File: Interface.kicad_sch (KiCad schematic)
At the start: 1 part, among them U3 USB3300-EZK-TR

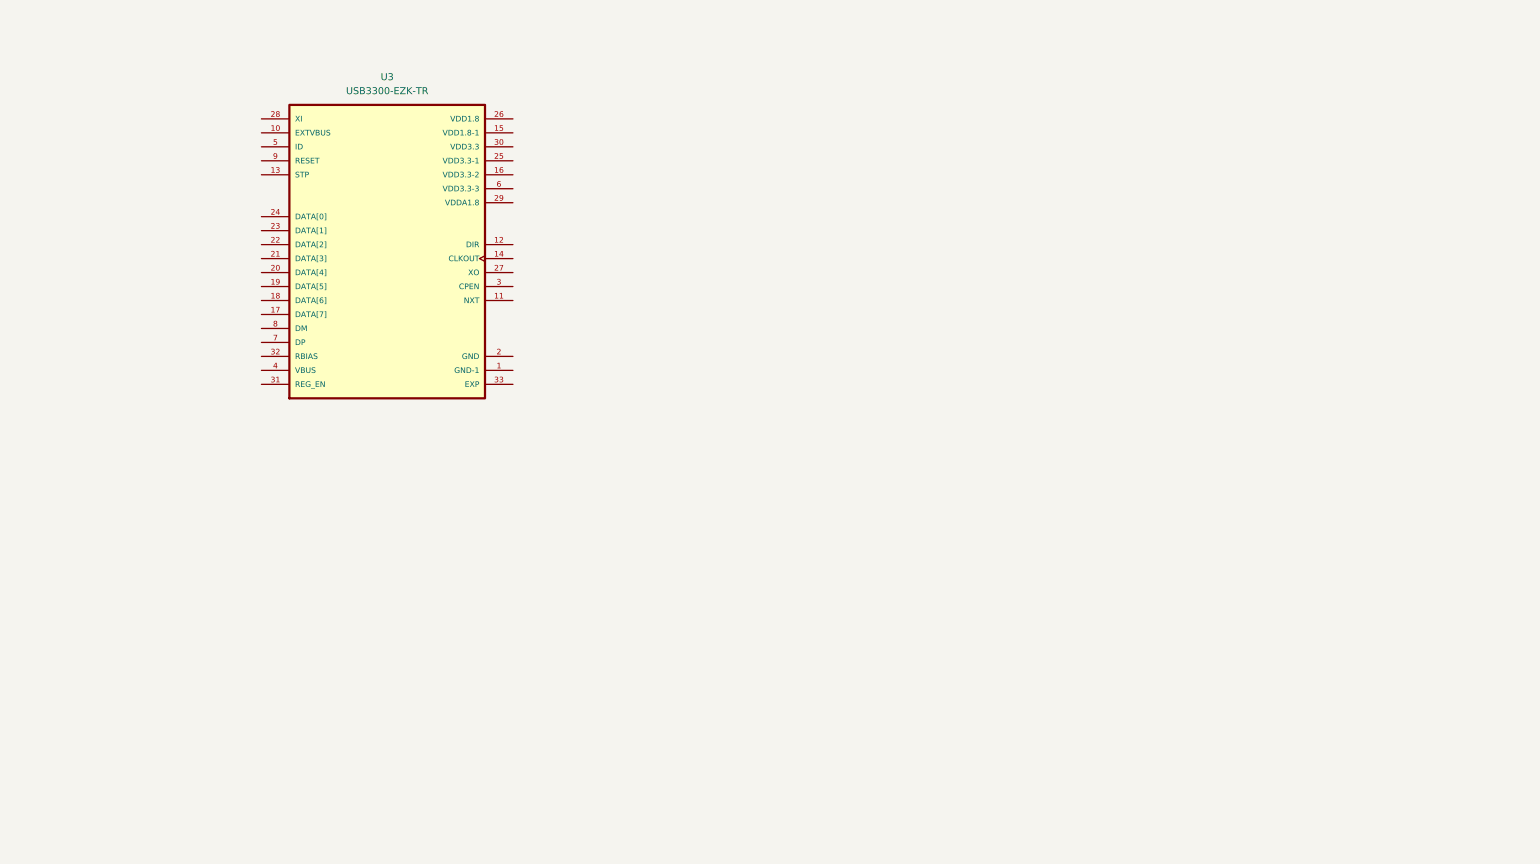
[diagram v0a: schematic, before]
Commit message: added USB (needs revision), fixed medium voltage rail
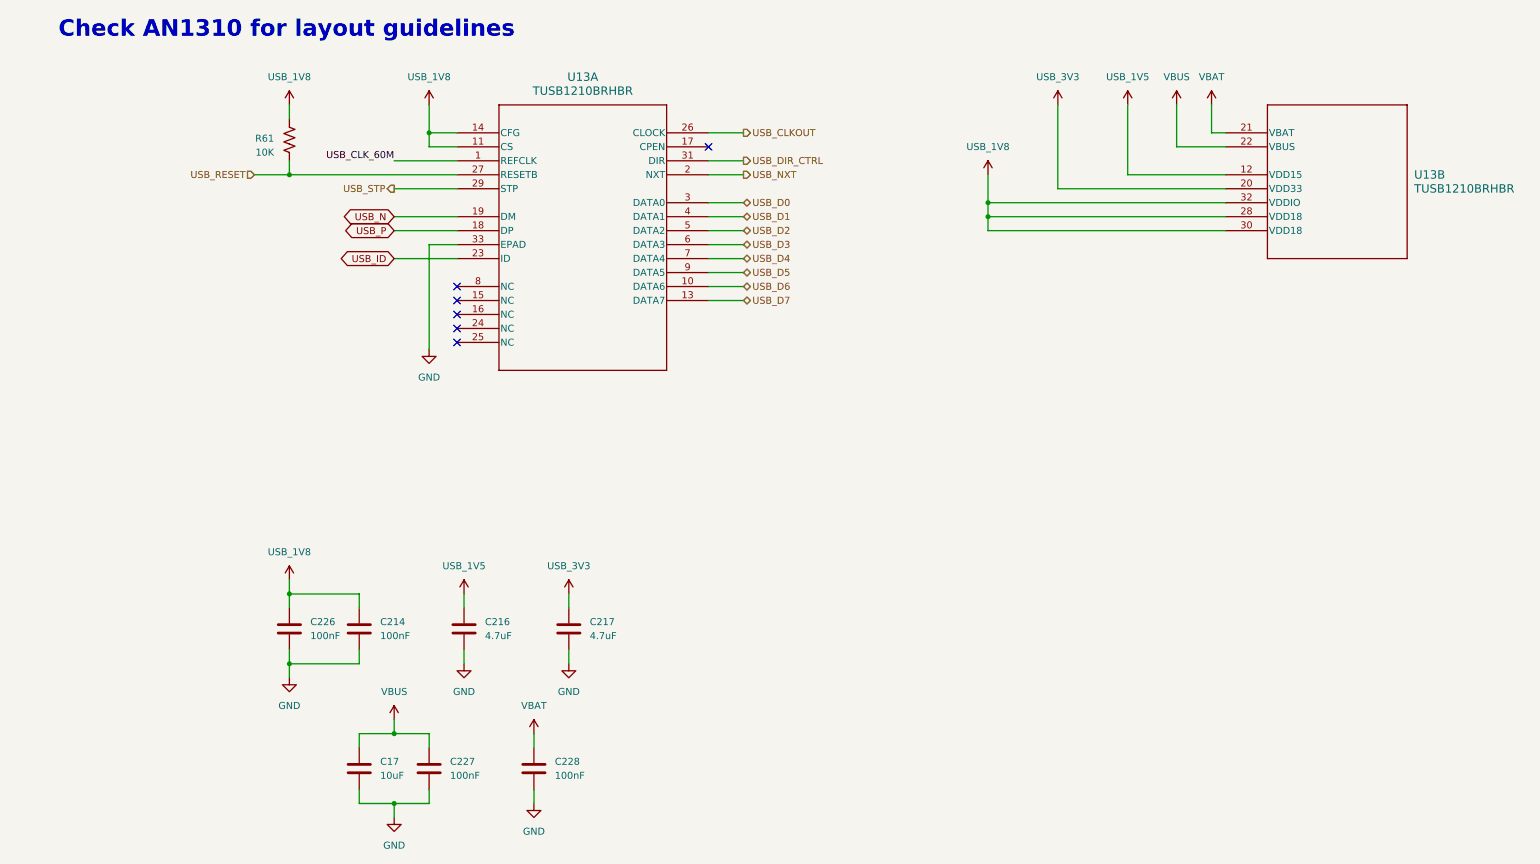
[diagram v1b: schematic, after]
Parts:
- removed U3: USB3300-EZK-TR, USB3300-EZK-TR:QFN50P500X500X100-33N, symbol USB3300-EZK-TR:USB3300-EZK-TR
- added C17: 10uF, symbol Device:C
- added C214, C226, C227, C228: 100nF, symbol Device:C
- added C216, C217: 4.7uF, symbol Device:C
- added R61: 10K, symbol Device:R_US
- added U13: TUSB1210BRHBR, RHB32_3P45X3P45, symbol TUSB1210BRHBR:TUSB1210BRHBR
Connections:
- new net GND: C17.2, C214.1, C216.1, C217.1, C226.1, C227.1, C228.1, U13.33 (EPAD)
- new net USB_1V5: C216.2, U13.12 (VDD15)
- new net USB_1V8: C214.2, C226.2, R61.1, U13.11 (CS), U13.14 (CFG), U13.28 (VDD18), U13.30 (VDD18), U13.32 (VDDIO)
- new net USB_3V3: C217.2, U13.20 (VDD33)
- new net USB_CLKOUT: U13.26 (CLOCK)
- new net USB_CLK_60M: U13.1 (REFCLK)
- new net USB_D0: U13.3 (DATA0)
- new net USB_D1: U13.4 (DATA1)
- new net USB_D2: U13.5 (DATA2)
- new net USB_D3: U13.6 (DATA3)
- new net USB_D4: U13.7 (DATA4)
- new net USB_D5: U13.9 (DATA5)
- new net USB_D6: U13.10 (DATA6)
- new net USB_D7: U13.13 (DATA7)
- new net USB_DIR_CTRL: U13.31 (DIR)
- new net USB_ID: U13.23 (ID)
- new net USB_N: U13.19 (DM)
- new net USB_NXT: U13.2 (NXT)
- new net USB_P: U13.18 (DP)
- new net USB_RESET: R61.2, U13.27 (RESETB)
- new net USB_STP: U13.29 (STP)
- new net VBAT: C228.2, U13.21 (VBAT)
- new net VBUS: C17.1, C227.2, U13.22 (VBUS)
- no-connect marks 0 -> 6
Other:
- note added: "Check AN1310 for layout guidelines"

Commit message: almost finished, phew! just dd +/- 5v rails, connect the SDIO & power enable pins and figure out the rest of the clocking chain
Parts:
- added C164, C166, C183: 100nF, symbol Device:C
- added C165: 1uF, symbol Device:C
- added FB9: BLM15AG601SN1D, symbol Device:FerriteBead
- added J3: 47352-1001, 47352-1001:MOLEX_47352-1001, symbol 47352-1001:47352-1001
- added R65: 100K, symbol Device:R_US
- added U10: USBLC6-2SC6, Package_TO_SOT_SMD:SOT-23-6, symbol Power_Protection:USBLC6-2SC6
- added U24: NVT4858HKZ, NVT4858_NXP, symbol NVT4858HKZ:NVT4858HKZ
- added Y2: TG-5006CG-12H_26.0000M3, TG5006CG12H260000M3, symbol TG-5006CG-12H_26_0000M3:TG-5006CG-12H_26.0000M3
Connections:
- net USB_CLK_60M is gone; now on net GND: U13.1 (REFCLK)
- net VBAT is gone; now on net USB_3V3: C228.2, U13.21 (VBAT)
- net GND: now also C164.2, C165.2, C166.2, C183.2, J3.6 (VSS), J3.S1 (SHIELD), J3.S2 (SHIELD__1), J3.S3 (SHIELD__2), J3.S4 (SHIELD__3), U10.2 (GND), U24.7 (GND), Y2.2 (GND)
- net USB_1V8: now also FB9.1, R65.1, U24.14 (VCCB)
- net USB_N: now also U10.1 (I/O1); no longer U13.19 (DM)
- net USB_P: now also U10.3 (I/O2); no longer U13.18 (DP)
- net VBUS: now also U10.5 (VBUS)
- net USB_CLKOUT renamed USB_26MHZ
- net USB_26MHZ: now also Y2.3 (OUT)
- new net SD_3V3: C164.1, C165.1, C166.1, J3.4 (VDD), U24.15 (VCCA)
- new net SD_CLK: U24.8 (CLKB)
- new net SD_CLK_PRE: J3.5 (CLK), U24.5 (CLKA)
- new net SD_CMD: U24.13 (CMDB)
- new net SD_CMD_PRE: J3.3 (CMD), U24.16 (CMDA)
- new net SD_DAT0: U24.10 (DAT0B)
- new net SD_DAT0_PRE: J3.7 (DATA0), U24.3 (DAT0A)
- new net SD_DAT1: U24.9 (DAT1B)
- new net SD_DAT1_PRE: J3.8 (DATA1), U24.4 (DAT1A)
- new net SD_DAT2: U24.12 (DAT2B)
- new net SD_DAT2_PRE: J3.1 (DATA2), U24.1 (DAT2A)
- new net SD_DAT3: U24.11 (DAT3B)
- new net SD_DAT3_PRE: J3.2 (CD/DATA3), U24.2 (DAT3A)
- new net SD_DETECT: J3.SW, R65.2
- new net USB_OSC_1V8: C183.1, FB9.2, Y2.4 (VCC)
- new net USB_PRE_N: U10.6 (I/O1), U13.19 (DM)
- new net USB_PRE_P: U10.4 (I/O2), U13.18 (DP)
- no-connect marks 6 -> 8
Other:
- note added: "3V3 & 1V5 are the outputs of internal LDOs"
- moved on the sheet: C17, C214, C216, C217, C226, C227, C228

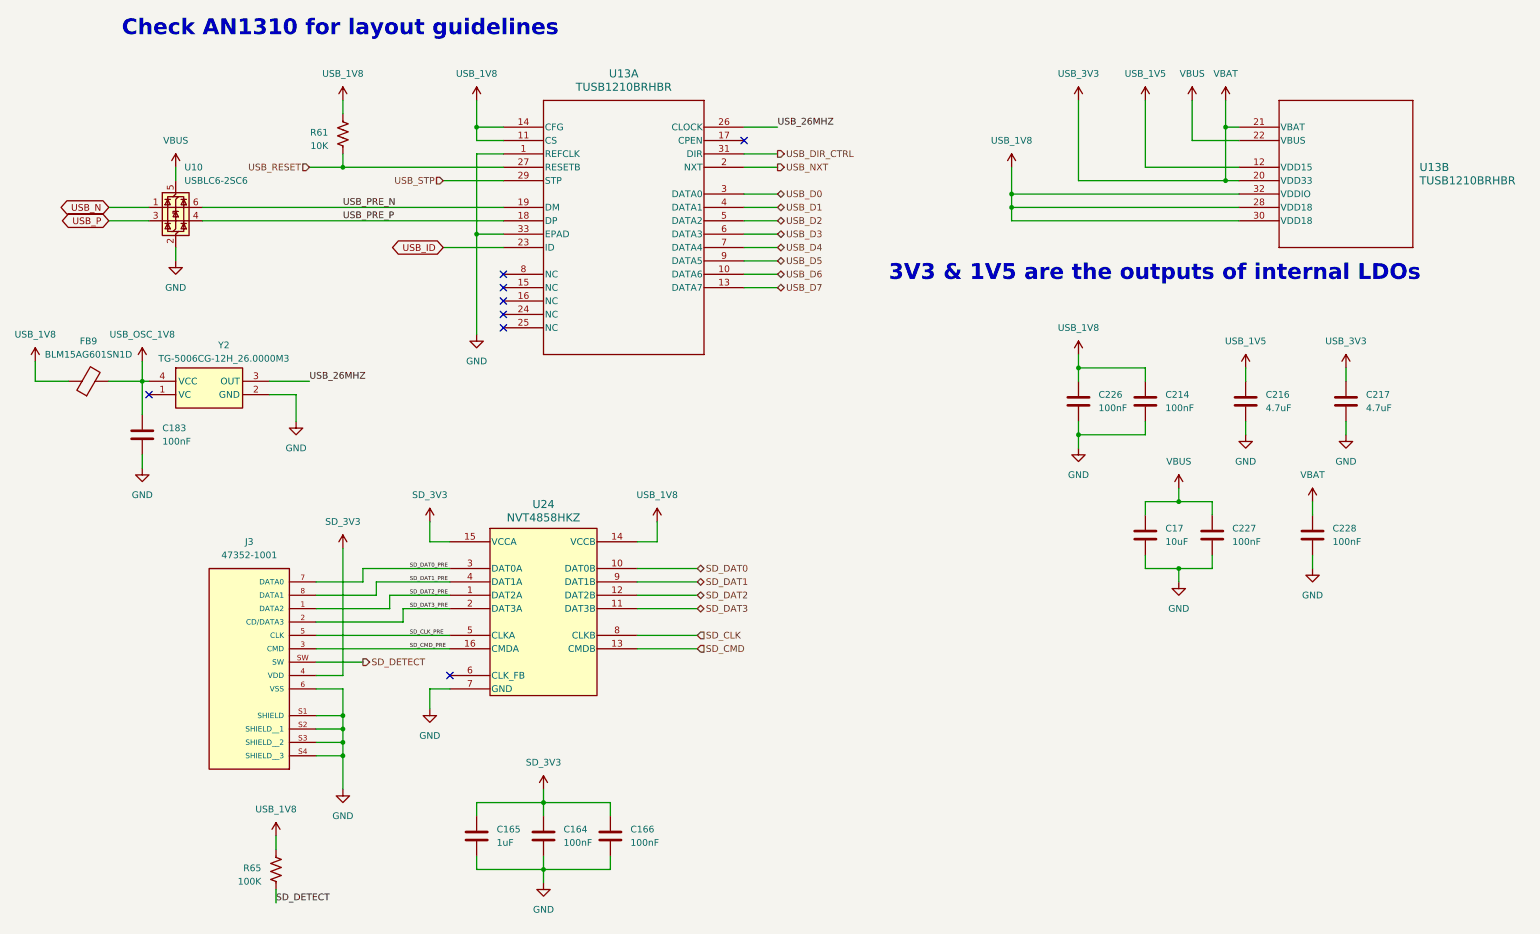
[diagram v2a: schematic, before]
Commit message: HDMI was requested so add it and give the signal chain a final revision
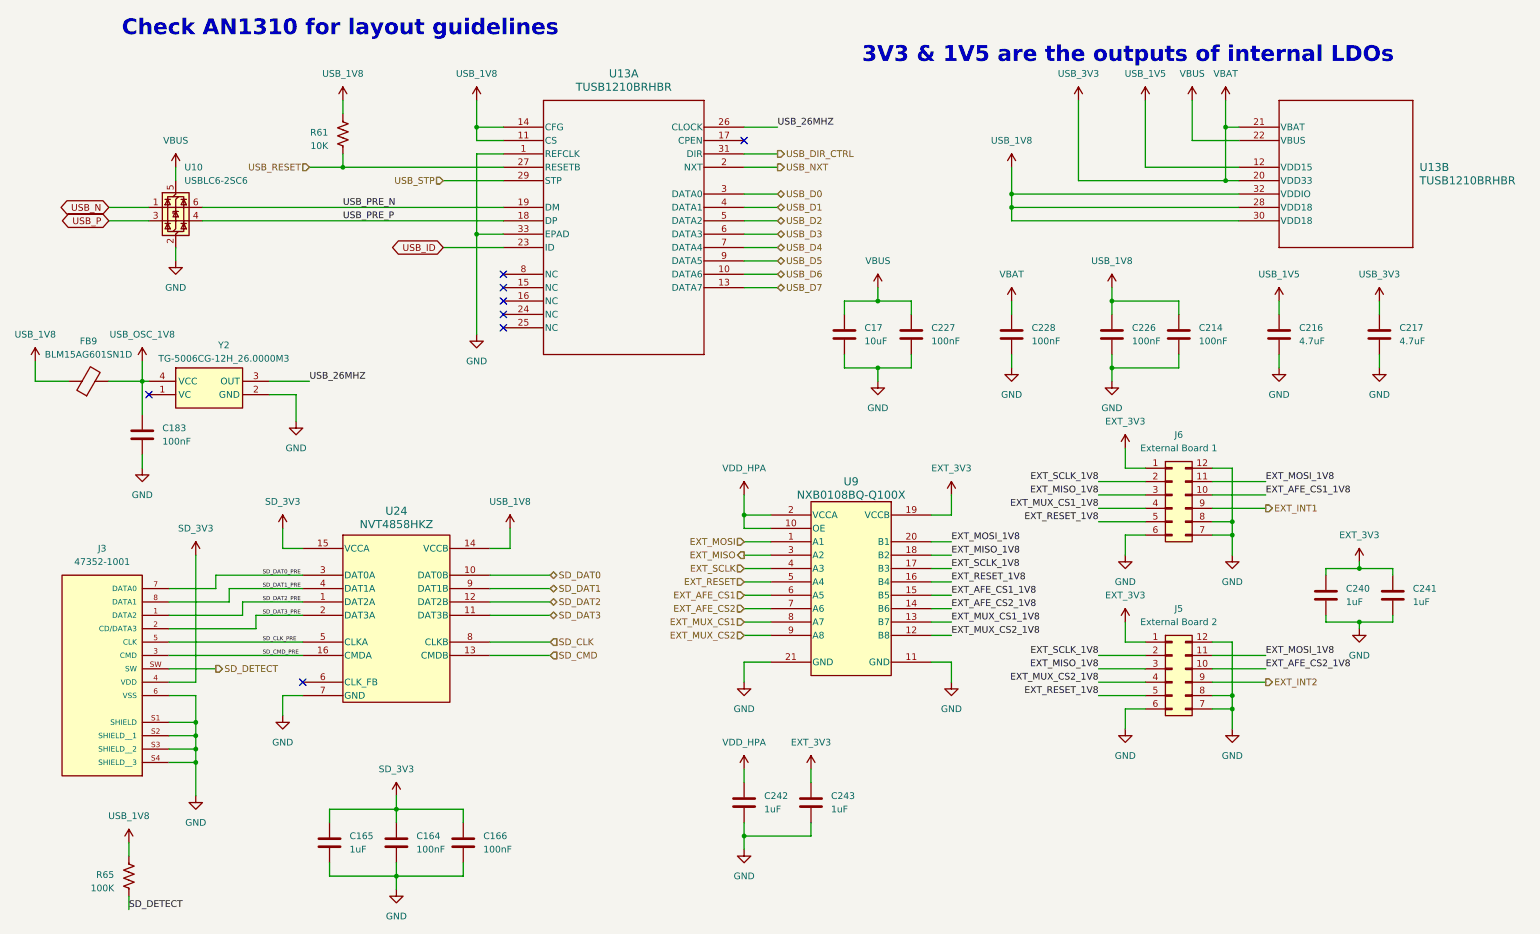
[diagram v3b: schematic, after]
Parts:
- added C240, C241, C242, C243: 1uF, symbol Device:C
- added J5: External Board 2, symbol Connector_Generic:Conn_02x06_Counter_Clockwise
- added J6: External Board 1, symbol Connector_Generic:Conn_02x06_Counter_Clockwise
- added U9: NXB0108BQ-Q100X, DHVQFN20_SOT764-1_NEX, symbol NXB0108BQ-Q100X:NXB0108BQ-Q100X
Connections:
- net GND: now also C240.2, C241.2, C242.2, C243.2, J5.12 (Pin_12), J5.6 (Pin_6), J5.7 (Pin_7), J5.8 (Pin_8), J6.12 (Pin_12), J6.6 (Pin_6), J6.7 (Pin_7), J6.8 (Pin_8), U9.11 (GND), U9.21 (GND)
- new net EXT_3V3: C240.1, C241.1, C243.1, J5.1 (Pin_1), J6.1 (Pin_1), U9.19 (VCCB)
- new net EXT_AFE_CS1: U9.6 (A5)
- new net EXT_AFE_CS1_1V8: J6.10 (Pin_10), U9.15 (B5)
- new net EXT_AFE_CS2: U9.7 (A6)
- new net EXT_AFE_CS2_1V8: J5.10 (Pin_10), U9.14 (B6)
- new net EXT_INT1: J6.9 (Pin_9)
- new net EXT_INT2: J5.9 (Pin_9)
- new net EXT_MISO: U9.3 (A2)
- new net EXT_MISO_1V8: J5.3 (Pin_3), J6.3 (Pin_3), U9.18 (B2)
- new net EXT_MOSI: U9.1 (A1)
- new net EXT_MOSI_1V8: J5.11 (Pin_11), J6.11 (Pin_11), U9.20 (B1)
- new net EXT_MUX_CS1: U9.8 (A7)
- new net EXT_MUX_CS1_1V8: J6.4 (Pin_4), U9.13 (B7)
- new net EXT_MUX_CS2: U9.9 (A8)
- new net EXT_MUX_CS2_1V8: J5.4 (Pin_4), U9.12 (B8)
- new net EXT_RESET: U9.5 (A4)
- new net EXT_RESET_1V8: J5.5 (Pin_5), J6.5 (Pin_5), U9.16 (B4)
- new net EXT_SCLK: U9.4 (A3)
- new net EXT_SCLK_1V8: J5.2 (Pin_2), J6.2 (Pin_2), U9.17 (B3)
- new net VDD_HPA: C242.1, U9.10 (OE), U9.2 (VCCA)
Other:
- moved on the sheet: C164, C165, C166, C17, C214, C216, C217, C226, C227, C228, J3, R65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

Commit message: ALL IS DONE EXCEPT HDMI PLEASE HELP
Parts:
- removed C17: 10uF, symbol Device:C
- removed C183: 100nF, symbol Device:C
- removed FB9: BLM15AG601SN1D, symbol Device:FerriteBead
- removed Y2: TG-5006CG-12H_26.0000M3, TG5006CG12H260000M3, symbol TG-5006CG-12H_26_0000M3:TG-5006CG-12H_26.0000M3
- added C246, C247, C248, C249, C250, C251, C252, C253, C254, C255, C256, C257, C258, C259, C260, C261: 100nF, symbol Device:C
- added C47: 47uF, symbol Device:C
- added CR1: DT1240A-08LP3810-7, U-DFN3810-9_TYPE_B_DIO, symbol DT1240A-08LP3810-7:DT1240A-08LP3810-7
- added J4: 2086581001, 2086581001:MOLEX_2086581001, symbol 2086581001:2086581001
- added J7: TYPE-C-31-M-12, TYPE-C-31-M-12:HRO_TYPE-C-31-M-12, symbol TYPE-C-31-M-12:TYPE-C-31-M-12
- added JP16: HPD_INV_PUP, U-DFN3810-9_TYPE_B_DIO, symbol Jumper:SolderJumper_2_Open
- added R106, R107, R67, R68, R85, R86, R87, R88: 10K, symbol Device:R_US
- added R109: 50R, symbol Device:R_US
- added R110, R111: 5.1K, symbol Device:R_US
- added R17: 4.02K, symbol Device:R_US
- added R69, R70, R83, R84: 3.3k, symbol Device:R_US
- added U18: SN75DP139RSBR, RSB40_3P15X3P15, symbol SN75DP139RSBR:SN75DP139RSBR
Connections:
- net GND: now also C246.2, C247.2, C248.2, C249.2, C250.2, C251.2, C252.2, C253.2, C47.2, CR1.3 (GND), J7.A1_B12 (GND), J7.B1_A12 (GND), J7.S1 (SHIELD), J7.S2 (SHIELD), J7.S3 (SHIELD), J7.S4 (SHIELD), R106.2, R110.2, R111.2, R17.2, R68.2, R86.2, R88.2, U18.41 (EPAD)
- net SD_3V3: now also U24.14 (VCCB); no longer U24.15 (VCCA)
- net SD_CLK: now also U24.5 (CLKA); no longer U24.8 (CLKB)
- net SD_CLK_PRE: now also U24.8 (CLKB); no longer U24.5 (CLKA)
- net SD_CMD: now also U24.16 (CMDA); no longer U24.13 (CMDB)
- net SD_CMD_PRE: now also U24.13 (CMDB); no longer U24.16 (CMDA)
- net SD_DAT0: now also U24.3 (DAT0A); no longer U24.10 (DAT0B)
- net SD_DAT0_PRE: now also U24.10 (DAT0B); no longer U24.3 (DAT0A)
- net SD_DAT1: now also U24.4 (DAT1A); no longer U24.9 (DAT1B)
- net SD_DAT1_PRE: now also U24.9 (DAT1B); no longer U24.4 (DAT1A)
- net SD_DAT2: now also U24.1 (DAT2A); no longer U24.12 (DAT2B)
- net SD_DAT2_PRE: now also U24.12 (DAT2B); no longer U24.1 (DAT2A)
- net SD_DAT3: now also U24.2 (DAT3A); no longer U24.11 (DAT3B)
- net SD_DAT3_PRE: now also U24.11 (DAT3B); no longer U24.2 (DAT3A)
- net USB_1V8: now also U24.15 (VCCA); no longer U24.14 (VCCB)
- net USB_26MHZ: now also R109.1; no longer U13.26 (CLOCK)
- net USB_N: now also J7.A7 (DN1), J7.B7 (DN2)
- net USB_P: now also J7.A6 (DP1), J7.B6 (DP2)
- net VBUS: now also C47.1, J7.A4_B9 (VBUS), J7.B4_A9 (VBUS)
- new net: U18.11 (NC), U18.20 (NC), U18.40 (NC)
- new net DP0_N: C255.1
- new net DP0_P: C254.1
- new net DP0_PRE_N: C255.2, U18.1 (IN_D1-)
- new net DP0_PRE_P: C254.2, U18.2 (IN_D1+)
- new net DP1_N: C257.1
- new net DP1_P: C256.1
- new net DP1_PRE_N: C257.2, U18.4 (IN_D2-)
- new net DP1_PRE_P: C256.2, U18.5 (IN_D2+)
- new net DP2_N: C259.1
- new net DP2_P: C258.1
- new net DP2_PRE_N: C259.2, U18.6 (IN_D3-)
- new net DP2_PRE_P: C258.2, U18.7 (IN_D3+)
- new net DP3_N: C261.1
- new net DP3_P: C260.1
- new net DP3_PRE_N: C261.2, U18.9 (IN_D4-)
- new net DP3_PRE_P: C260.2, U18.10 (IN_D4+)
- new net HDMI_3V3: C246.1, C247.1, C248.1, C249.1, C250.1, C251.1, C252.1, C253.1, JP16.1 (A), R107.1, R67.1, R69.1, R70.1, R85.1, R87.1, U18.12 (VCC), U18.19 (VCCC), U18.23 (VCC), U18.28 (VCC), U18.3 (VCC), U18.32 (VCC), U18.37 (VCC), U18.8 (VCC)
- new net HDMI_5V: R83.1, R84.1
- new net HDMI_D0_N: CR1.6 (LINE-7), U18.30 (OUT_D1-)
- new net HDMI_D0_P: CR1.5 (LINE-8), U18.29 (OUT_D1+)
- new net HDMI_D1_N: CR1.7 (LINE-5), U18.27 (OUT_D2-)
- new net HDMI_D1_P: CR1.4 (LINE-6), U18.26 (OUT_D2+)
- new net HDMI_D2_N: CR1.2 (LINE-3), U18.25 (OUT_D3-)
- new net HDMI_D2_P: CR1.8 (LINE-4), U18.24 (OUT_D3+)
- new net HDMI_D3_N: CR1.1 (LINE-1), U18.22 (OUT_D4-)
- new net HDMI_D3_P: CR1.9 (LINE-2), U18.21 (OUT_D4+)
- new net HDMI_DDC_EN: R85.2, U18.36 (DDC_EN)
- new net HDMI_HPDINV: JP16.2 (B), R86.1, U18.38 (HPDINV)
- new net HDMI_HPD_CONN: U18.35 (HPD_SINK)
- new net HDMI_HPD_SOM: R106.1, U18.16 (HPD_SOURCE)
- new net HDMI_I2C_EN: R67.2, U18.14 (I2C_EN)
- new net HDMI_I2C_SCL_CONN: R84.2, U18.33 (SCL_SINK)
- new net HDMI_I2C_SCL_SOM: R69.2, U18.18 (SCL_SOURCE)
- new net HDMI_I2C_SDA_CONN: R83.2, U18.34 (SDA_SINK)
- new net HDMI_I2C_SDA_SOM: R70.2, U18.17 (SDA_SOURCE)
- new net HDMI_OEn: R68.1, U18.31 (OE_N)
- new net HDMI_OVS: R107.2, U18.39 (OVS)
- new net HDMI_SRC: R87.2, R88.1, U18.13 (SRC)
- new net HDMI_VSADJ: R17.1, U18.15 (VSADJ)
- new net USB_CC1: J7.A5 (CC1), R111.1
- new net USB_CC2: J7.B5 (CC2), R110.1
- new net USB_CLK: R109.2, U13.26 (CLOCK)
- no-connect marks 8 -> 10
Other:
- added sheet DP2HDMI (DP2HDMI.kicad_sch)
- note added: "Common SPI & Control Lines - MOSI - MISO - SCLK - RESET Seperate SPI Pins: - AFE CS - MUX CS"
- note added: "External Modules Connectors"
- note added: "Level conversion 3V3 <-> 1V8"
- note added: "SD Card"
- note added: "USB HS PHY"
- moved on the sheet: C164, C165, C166, C240, C241, C242, C243, J3, J5, J6, R61, R65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
